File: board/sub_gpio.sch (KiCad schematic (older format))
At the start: 0 parts

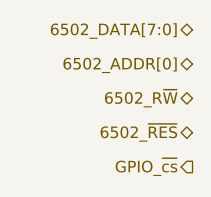
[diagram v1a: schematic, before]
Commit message: Level converters complete, display almost done
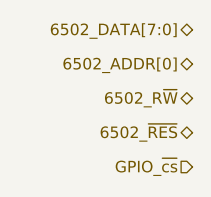
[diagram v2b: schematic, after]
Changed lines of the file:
@@
 $Descr A4 11693 8268
 encoding utf-8
-Sheet 4 10
+Sheet 4 15
 Title ""
 Date ""
@@
 Comment2 ""
 Comment3 ""
-Comment4 ""
+Comment4 "Quokka 6502 Microprocessor Trainer"
 $EndDescr
 Text HLabel 3650 1950 0    50   3State ~ 0
@@
 Text HLabel 3650 2100 0    50   BiDi ~ 0
 6502_ADDR[0]
-Text HLabel 3650 2550 0    50   Output ~ 0
+Text HLabel 3650 2550 0    50   Input ~ 0
 GPIO_~cs
 Text HLabel 3650 2400 0    50   BiDi ~ 0

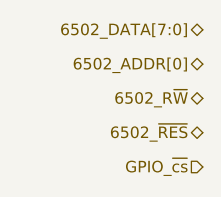
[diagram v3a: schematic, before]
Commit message: Bus signal connectivity rebuilt
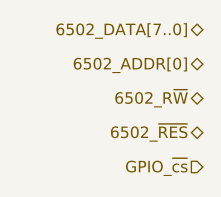
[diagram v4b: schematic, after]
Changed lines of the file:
@@
 $EndDescr
 Text HLabel 3650 1950 0    50   3State ~ 0
-6502_DATA[7:0]
+6502_DATA[7..0]
 Text HLabel 3650 2250 0    50   BiDi ~ 0
 6502_R~W

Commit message: gpio done
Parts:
- added C401, C?: 1u, symbol Device:C
- added D401, D?: DF5A6.8F, Package_TO_SOT_SMD:SOT-353_SC-70-5, symbol Power_Protection:SP0504BAJT
- added D402, D403, D404, D405, D406, D407, D408, D409: LED_Small, symbol Device:LED_Small
- added J401: Conn_01x08, symbol Connector_Generic:Conn_01x08
- added R401, R402, R403, R404, R405, R406, R407, R408: 160, symbol Device:R
- added U401: 74LVC4245A, symbol quokka:74LVC4245A
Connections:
- new net: D409.2 (A), D?.1 (K), J401.1 (Pin_1), U401.10 (GND)
- new net: D401.5 (K), D402.2 (A), J401.8 (Pin_8), U401.3 (A0)
- new net: D401.4 (K), D403.2 (A), J401.7 (Pin_7), U401.4 (A1)
- new net: D401.3 (K), D404.2 (A), J401.6 (Pin_6), U401.5 (A2)
- new net: D401.1 (K), D405.2 (A), J401.5 (Pin_5), U401.6 (A3)
- new net: D406.2 (A), D?.5 (K), J401.4 (Pin_4), U401.7 (A4)
- new net: D407.2 (A), D?.4 (K), J401.3 (Pin_3), U401.8 (A5)
- new net: D408.2 (A), D?.3 (K), J401.2 (Pin_2), U401.9 (A6)
- new net: D402.1 (K), R401.1
- new net: D409.1 (K), R408.1
- new net: D408.1 (K), R407.1
- new net: D407.1 (K), R406.1
- new net: D406.1 (K), R405.1
- new net: D405.1 (K), R404.1
- new net: D404.1 (K), R403.1
- new net: D403.1 (K), R402.1
- new net +3V3: C?.1, U401.23 (VCCB), U401.24 (VCCB)
- new net +5V: C401.1, U401.1 (VCCA)
- new net G0: U401.21 (B0)
- new net G1: U401.20 (B1)
- new net G2: U401.19 (B2)
- new net G3: U401.18 (B3)
- new net G4: U401.17 (B4)
- new net G5: U401.16 (B5)
- new net G6: U401.15 (B6)
- new net G7: U401.14 (B7)
- new net GND: C401.2, C?.2, D401.2 (A), D?.2 (A), R401.2, R402.2, R403.2, R404.2, R405.2, R406.2, R407.2, R408.2, U401.10 (GND), U401.12 (GND), U401.13 (GND), U401.22 (CE)
- new net R~W: U401.2 (A->B)
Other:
- note added: "Bidirectional Data"

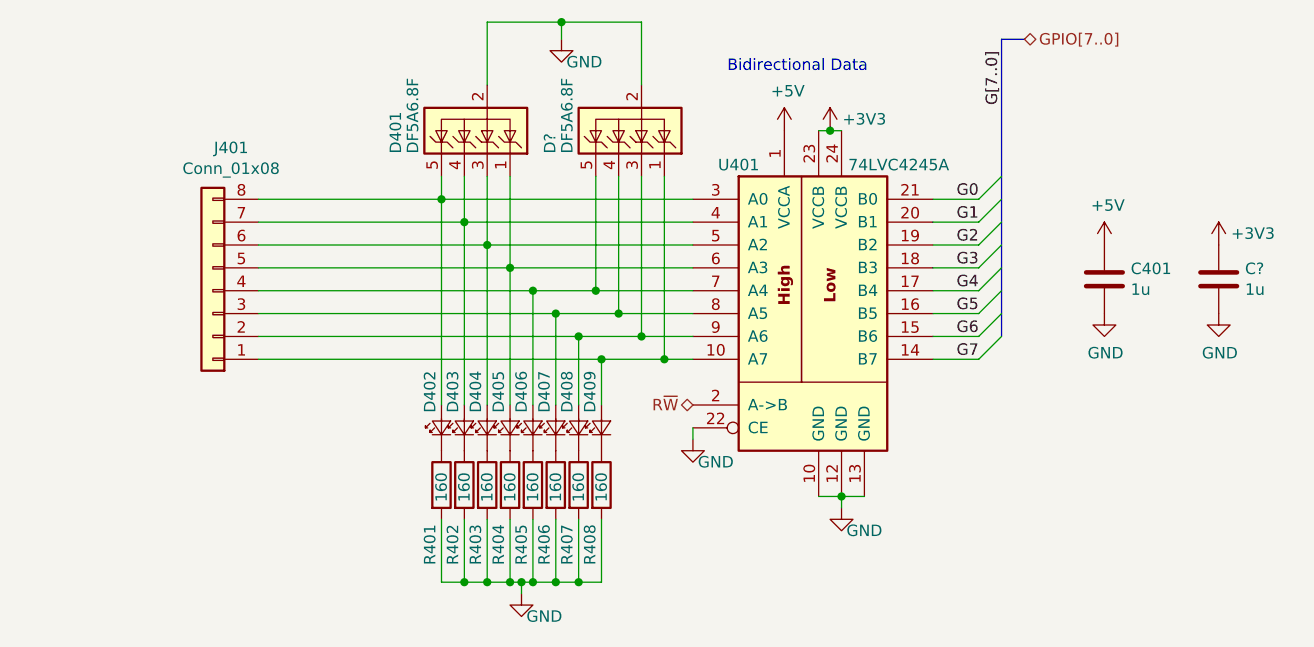
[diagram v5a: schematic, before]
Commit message: made some changes based on projected power budget
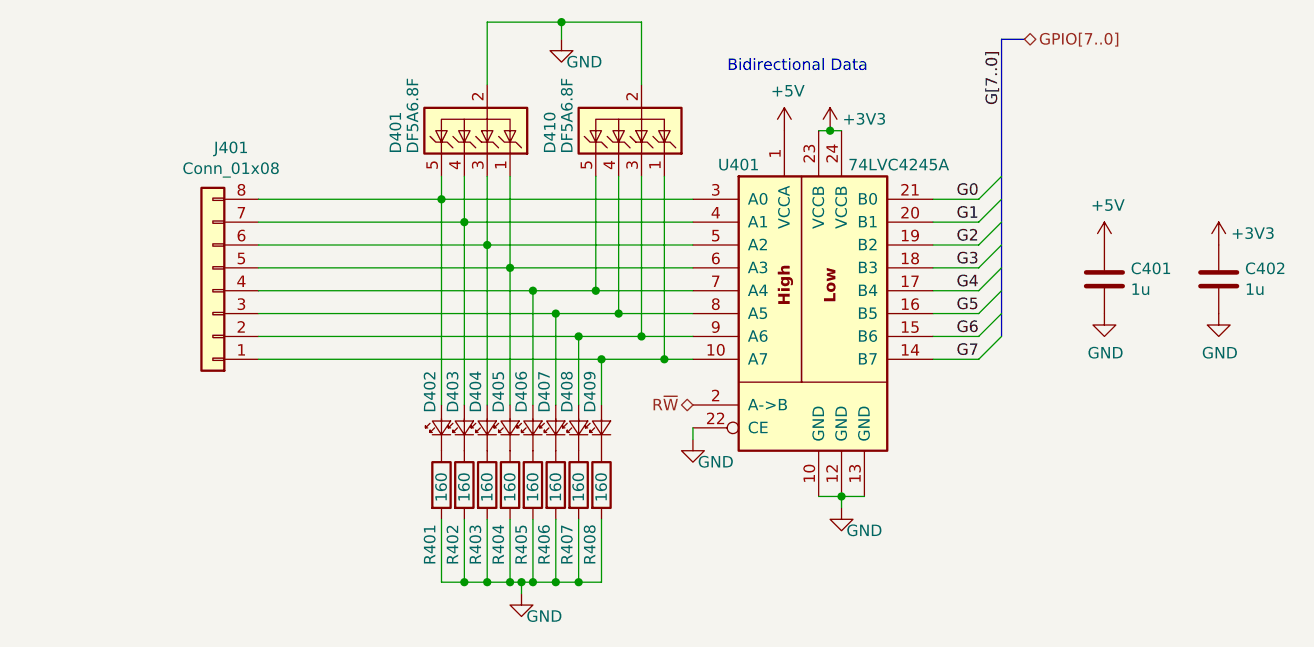
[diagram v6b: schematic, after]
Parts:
- gave numbers to parts that had none: 2
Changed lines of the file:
@@
 $EndComp
 $Comp
-L Power_Protection:SP0504BAJT D?
+L Power_Protection:SP0504BAJT D410
 U 1 1 5ABECE71
 P 4775 2200
-F 0 "D?" V 5175 2300 50  0000 R CNN
+F 0 "D410" V 5175 2300 50  0000 R CNN
 F 1 "DF5A6.8F" V 5100 2300 50  0000 R CNN
 F 2 "Package_TO_SOT_SMD:SOT-353_SC-70-5" H 5075 2150 50  0001 L CNN
@@
 	3900 2400 3900 2500
 $Comp
-L power:GND #PWR?
+L power:GND #PWR0408
 U 1 1 5AC0745E
 P 4425 1800
-F 0 "#PWR?" H 4425 1550 50  0001 C CNN
+F 0 "#PWR0408" H 4425 1550 50  0001 C CNN
 F 1 "GND" H 4525 1700 50  0000 C CNN
 F 2 "" H 4425 1800 50  0001 C CNN
@@
 Connection ~ 4425 1725
 $Comp
-L power:GND #PWR?
+L power:GND #PWR0407
 U 1 1 5AC0C5ED
 P 4250 4225
-F 0 "#PWR?" H 4250 3975 50  0001 C CNN
+F 0 "#PWR0407" H 4250 3975 50  0001 C CNN
 F 1 "GND" H 4350 4125 50  0000 C CNN
 F 2 "" H 4250 4225 50  0001 C CNN
@@
 	4250 4175 4300 4175
 $Comp
-L Device:C C?
+L Device:C C402
 U 1 1 5AC1AF1D
 P 7300 2850
-F 0 "C?" H 7415 2896 50  0000 L CNN
+F 0 "C402" H 7415 2896 50  0000 L CNN
 F 1 "1u" H 7415 2805 50  0000 L CNN
 F 2 "" H 7338 2700 50  0001 C CNN
@@
 $EndComp
 $Comp
-L power:GND #PWR?
+L power:GND #PWR0410
 U 1 1 5AC1AF23
 P 7300 3000
-F 0 "#PWR?" H 7300 2750 50  0001 C CNN
+F 0 "#PWR0410" H 7300 2750 50  0001 C CNN
 F 1 "GND" H 7305 2827 50  0000 C CNN
 F 2 "" H 7300 3000 50  0001 C CNN
@@
 	1    0    0    -1
 $EndComp
-Wire Bus Line
-	6350 1800 6350 3100
-$Comp
-L power:+3V3 #PWR?
+$Comp
+L power:+3V3 #PWR0409
 U 1 1 5AC1C826
 P 7300 2700
-F 0 "#PWR?" H 7300 2550 50  0001 C CNN
+F 0 "#PWR0409" H 7300 2550 50  0001 C CNN
 F 1 "+3V3" H 7450 2750 50  0000 C CNN
 F 2 "" H 7300 2700 50  0001 C CNN
@@
 	1    0    0    -1
 $EndComp
+Wire Bus Line
+	6350 1800 6350 3100
 $EndSCHEMATC

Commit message: Schematics mostly complete
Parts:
- removed J401: Conn_01x08, symbol Connector_Generic:Conn_01x08
- added J401: Conn_01x09, symbol Connector_Generic:Conn_01x09
- R401, R402, R403, R404, R405, R406, R407, R408: value 160 -> 390
- renumbered D410 to D402, D402 to D403, D403 to D404, D404 to D405, D405 to D406, D406 to D407, D407 to D408, D408 to D409, D409 to D410
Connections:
- net GND: now also J401.9 (Pin_9)
- net at D402.1 (K), D410.2 (A), U401.10 (GND): now also J401.8 (Pin_8)
- net at D401.5 (K), D403.2 (A), U401.3 (A0): now also J401.1 (Pin_1)
- net at D401.4 (K), D404.2 (A), U401.4 (A1): now also J401.2 (Pin_2)
- net at D401.3 (K), D405.2 (A), U401.5 (A2): now also J401.3 (Pin_3)
- net at D401.1 (K), D406.2 (A), U401.6 (A3): now also J401.4 (Pin_4)
- net at D402.5 (K), D407.2 (A), U401.7 (A4): now also J401.5 (Pin_5)
- net at D402.4 (K), D408.2 (A), U401.8 (A5): now also J401.6 (Pin_6)
- net at D402.3 (K), D409.2 (A), U401.9 (A6): now also J401.7 (Pin_7)
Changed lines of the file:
@@
 GPIO[7..0]
 $Comp
-L power:GND #PWR0404
+L power:GND #PWR0410
 U 1 1 5ABD3089
 P 5650 3850
-F 0 "#PWR0404" H 5650 3600 50  0001 C CNN
+F 0 "#PWR0410" H 5650 3600 50  0001 C CNN
 F 1 "GND" H 5750 3750 50  0000 C CNN
 F 2 "" H 5650 3850 50  0001 C CNN
@@
 G[7..0]
 $Comp
-L power:GND #PWR0401
+L power:GND #PWR0409
 U 1 1 5ABD3633
 P 5000 3550
-F 0 "#PWR0401" H 5000 3300 50  0001 C CNN
+F 0 "#PWR0409" H 5000 3300 50  0001 C CNN
 F 1 "GND" H 5100 3450 50  0000 C CNN
 F 2 "" H 5000 3550 50  0001 C CNN
@@
 $EndComp
 $Comp
-L power:+5V #PWR0405
+L power:+5V #PWR0404
 U 1 1 5ABD4DE4
 P 6800 2700
-F 0 "#PWR0405" H 6800 2550 50  0001 C CNN
+F 0 "#PWR0404" H 6800 2550 50  0001 C CNN
 F 1 "+5V" H 6815 2873 50  0000 C CNN
 F 2 "" H 6800 2700 50  0001 C CNN
@@
 $EndComp
 $Comp
-L Connector_Generic:Conn_01x08 J401
-U 1 1 5ABD5411
-P 2900 2900
-F 0 "J401" H 2820 2275 50  0000 C CNN
-F 1 "Conn_01x08" H 2820 2366 50  0000 C CNN
-F 2 "" H 2900 2900 50  0001 C CNN
-F 3 "~" H 2900 2900 50  0001 C CNN
-	1    2900 2900
-	-1   0    0    1
-$EndComp
-$Comp
-L Device:LED_Small D402
+L Device:LED_Small D403
 U 1 1 5ABE75BA
 P 3900 3500
-F 0 "D402" H 4150 3550 50  0000 R CNN
+F 0 "D403" H 4150 3550 50  0000 R CNN
 F 1 "LED_Small" V 3855 3432 50  0001 R CNN
 F 2 "" V 3900 3500 50  0001 C CNN
@@
 $EndComp
 $Comp
-L Device:LED_Small D409
+L Device:LED_Small D410
 U 1 1 5ABE75EB
 P 4600 3500
-F 0 "D409" H 4850 3550 50  0000 R CNN
+F 0 "D410" H 4850 3550 50  0000 R CNN
 F 1 "LED_Small" V 4555 3432 50  0001 R CNN
 F 2 "" V 4600 3500 50  0001 C CNN
@@
 $EndComp
 $Comp
-L Device:LED_Small D408
+L Device:LED_Small D409
 U 1 1 5ABE75F2
 P 4500 3500
-F 0 "D408" H 4750 3550 50  0000 R CNN
+F 0 "D409" H 4750 3550 50  0000 R CNN
 F 1 "LED_Small" V 4455 3432 50  0001 R CNN
 F 2 "" V 4500 3500 50  0001 C CNN
@@
 $EndComp
 $Comp
-L Device:LED_Small D407
+L Device:LED_Small D408
 U 1 1 5ABE75F9
 P 4400 3500
-F 0 "D407" H 4650 3550 50  0000 R CNN
+F 0 "D408" H 4650 3550 50  0000 R CNN
 F 1 "LED_Small" V 4355 3432 50  0001 R CNN
 F 2 "" V 4400 3500 50  0001 C CNN
@@
 $EndComp
 $Comp
-L Device:LED_Small D406
+L Device:LED_Small D407
 U 1 1 5ABE7600
 P 4300 3500
-F 0 "D406" H 4550 3550 50  0000 R CNN
+F 0 "D407" H 4550 3550 50  0000 R CNN
 F 1 "LED_Small" V 4255 3432 50  0001 R CNN
 F 2 "" V 4300 3500 50  0001 C CNN
@@
 $EndComp
 $Comp
-L Device:LED_Small D405
+L Device:LED_Small D406
 U 1 1 5ABE7607
 P 4200 3500
-F 0 "D405" H 4450 3550 50  0000 R CNN
+F 0 "D406" H 4450 3550 50  0000 R CNN
 F 1 "LED_Small" V 4155 3432 50  0001 R CNN
 F 2 "" V 4200 3500 50  0001 C CNN
@@
 $EndComp
 $Comp
-L Device:LED_Small D404
+L Device:LED_Small D405
 U 1 1 5ABE760E
 P 4100 3500
-F 0 "D404" H 4350 3550 50  0000 R CNN
+F 0 "D405" H 4350 3550 50  0000 R CNN
 F 1 "LED_Small" V 4055 3432 50  0001 R CNN
 F 2 "" V 4100 3500 50  0001 C CNN
@@
 $EndComp
 $Comp
-L Device:LED_Small D403
+L Device:LED_Small D404
 U 1 1 5ABE7615
 P 4000 3500
-F 0 "D403" H 4250 3550 50  0000 R CNN
+F 0 "D404" H 4250 3550 50  0000 R CNN
 F 1 "LED_Small" V 3955 3432 50  0001 R CNN
 F 2 "" V 4000 3500 50  0001 C CNN
@@
 P 3900 3750
 F 0 "R401" V 3850 3400 50  0000 L CNN
-F 1 "160" V 3900 3675 50  0000 L CNN
+F 1 "390" V 3900 3675 50  0000 L CNN
 F 2 "" V 3830 3750 50  0001 C CNN
 F 3 "~" H 3900 3750 50  0001 C CNN
@@
 P 4000 3750
 F 0 "R402" V 3950 3400 50  0000 L CNN
-F 1 "160" V 4000 3675 50  0000 L CNN
+F 1 "390" V 4000 3675 50  0000 L CNN
 F 2 "" V 3930 3750 50  0001 C CNN
 F 3 "~" H 4000 3750 50  0001 C CNN
@@
 P 4100 3750
 F 0 "R403" V 4050 3400 50  0000 L CNN
-F 1 "160" V 4100 3675 50  0000 L CNN
+F 1 "390" V 4100 3675 50  0000 L CNN
 F 2 "" V 4030 3750 50  0001 C CNN
 F 3 "~" H 4100 3750 50  0001 C CNN
@@
 P 4200 3750
 F 0 "R404" V 4150 3400 50  0000 L CNN
-F 1 "160" V 4200 3675 50  0000 L CNN
+F 1 "390" V 4200 3675 50  0000 L CNN
 F 2 "" V 4130 3750 50  0001 C CNN
 F 3 "~" H 4200 3750 50  0001 C CNN
@@
 P 4300 3750
 F 0 "R405" V 4250 3400 50  0000 L CNN
-F 1 "160" V 4300 3675 50  0000 L CNN
+F 1 "390" V 4300 3675 50  0000 L CNN
 F 2 "" V 4230 3750 50  0001 C CNN
 F 3 "~" H 4300 3750 50  0001 C CNN
@@
 P 4400 3750
 F 0 "R406" V 4350 3400 50  0000 L CNN
-F 1 "160" V 4400 3675 50  0000 L CNN
+F 1 "390" V 4400 3675 50  0000 L CNN
 F 2 "" V 4330 3750 50  0001 C CNN
 F 3 "~" H 4400 3750 50  0001 C CNN
@@
 P 4500 3750
 F 0 "R407" V 4450 3400 50  0000 L CNN
-F 1 "160" V 4500 3675 50  0000 L CNN
+F 1 "390" V 4500 3675 50  0000 L CNN
 F 2 "" V 4430 3750 50  0001 C CNN
 F 3 "~" H 4500 3750 50  0001 C CNN
@@
 P 4600 3750
 F 0 "R408" V 4550 3400 50  0000 L CNN
-F 1 "160" V 4600 3675 50  0000 L CNN
+F 1 "390" V 4600 3675 50  0000 L CNN
 F 2 "" V 4530 3750 50  0001 C CNN
 F 3 "~" H 4600 3750 50  0001 C CNN
@@
 $EndComp
 $Comp
-L Power_Protection:SP0504BAJT D410
+L Power_Protection:SP0504BAJT D402
 U 1 1 5ABECE71
 P 4775 2200
-F 0 "D410" V 5175 2300 50  0000 R CNN
+F 0 "D402" V 5175 2300 50  0000 R CNN
 F 1 "DF5A6.8F" V 5100 2300 50  0000 R CNN
 F 2 "Package_TO_SOT_SMD:SOT-353_SC-70-5" H 5075 2150 50  0001 L CNN
@@
 	3900 2400 3900 2500
 $Comp
-L power:GND #PWR0408
+L power:GND #PWR0401
 U 1 1 5AC0745E
 P 4425 1800
-F 0 "#PWR0408" H 4425 1550 50  0001 C CNN
+F 0 "#PWR0401" H 4425 1550 50  0001 C CNN
 F 1 "GND" H 4525 1700 50  0000 C CNN
 F 2 "" H 4425 1800 50  0001 C CNN
@@
 Connection ~ 4425 1725
 $Comp
-L power:GND #PWR0407
+L power:GND #PWR0411
 U 1 1 5AC0C5ED
 P 4250 4225
-F 0 "#PWR0407" H 4250 3975 50  0001 C CNN
+F 0 "#PWR0411" H 4250 3975 50  0001 C CNN
 F 1 "GND" H 4350 4125 50  0000 C CNN
 F 2 "" H 4250 4225 50  0001 C CNN
@@
 $EndComp
 $Comp
-L power:GND #PWR0410
+L power:GND #PWR0407
 U 1 1 5AC1AF23
 P 7300 3000
-F 0 "#PWR0410" H 7300 2750 50  0001 C CNN
+F 0 "#PWR0407" H 7300 2750 50  0001 C CNN
 F 1 "GND" H 7305 2827 50  0000 C CNN
 F 2 "" H 7300 3000 50  0001 C CNN
@@
 $EndComp
 $Comp
-L power:+3V3 #PWR0409
+L power:+3V3 #PWR0405
 U 1 1 5AC1C826
 P 7300 2700
-F 0 "#PWR0409" H 7300 2550 50  0001 C CNN
-F 1 "+3V3" H 7450 2750 50  0000 C CNN
+F 0 "#PWR0405" H 7300 2550 50  0001 C CNN
+F 1 "+3V3" H 7300 2875 50  0000 C CNN
 F 2 "" H 7300 2700 50  0001 C CNN
 F 3 "" H 7300 2700 50  0001 C CNN
@@
 	1    0    0    -1
 $EndComp
+$Comp
+L Connector_Generic:Conn_01x09 J401
+U 1 1 5ACF6504
+P 2900 2900
+F 0 "J401" H 2820 3517 50  0000 C CNN
+F 1 "Conn_01x09" H 2820 3426 50  0000 C CNN
+F 2 "" H 2900 2900 50  0001 C CNN
+F 3 "~" H 2900 2900 50  0001 C CNN
+	1    2900 2900
+	-1   0    0    -1
+$EndComp
+$Comp
+L power:GND #PWR0408
+U 1 1 5ACF822D
+P 3150 3350
+F 0 "#PWR0408" H 3150 3100 50  0001 C CNN
+F 1 "GND" H 3155 3177 50  0000 C CNN
+F 2 "" H 3150 3350 50  0001 C CNN
+F 3 "" H 3150 3350 50  0001 C CNN
+	1    3150 3350
+	1    0    0    -1
+$EndComp
+Wire Wire Line
+	3150 3350 3150 3300
+Wire Wire Line
+	3150 3300 3100 3300
 Wire Bus Line
 	6350 1800 6350 3100

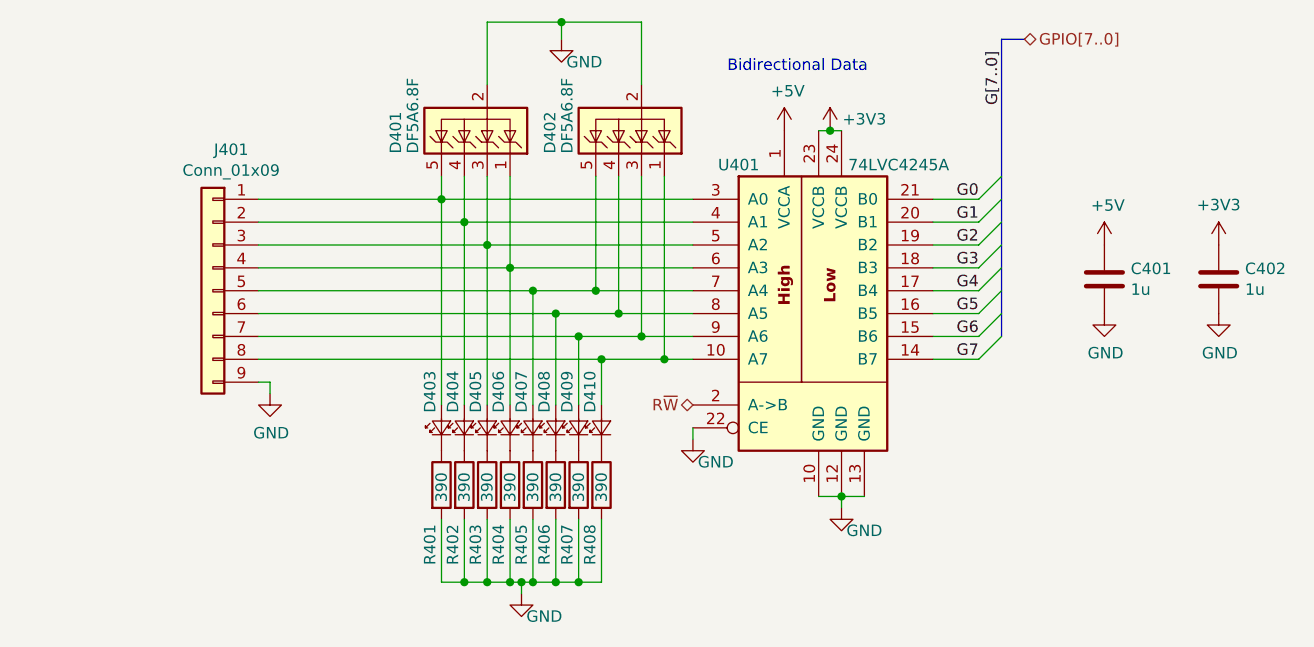
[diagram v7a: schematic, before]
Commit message: Started picking footprints. Merged many components.
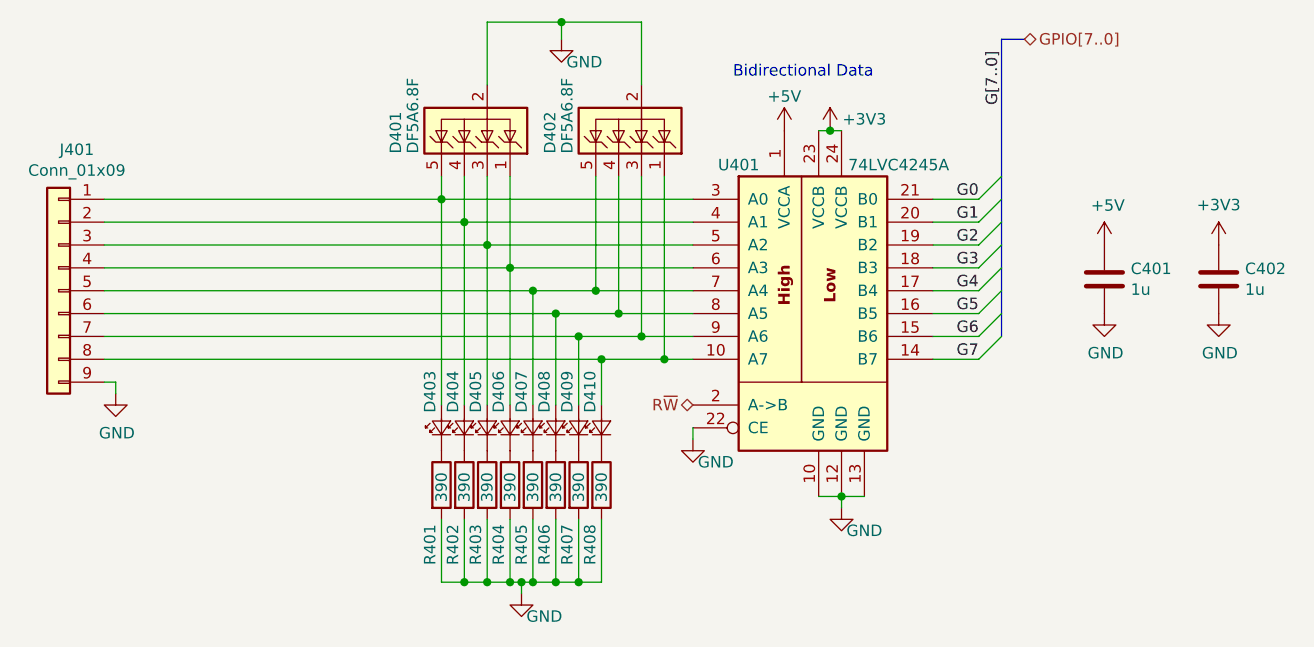
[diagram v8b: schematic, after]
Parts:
- U401: footprint (none) -> Package_SO:TSSOP-24_4.4x7.8mm_P0.65mm
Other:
- moved on the sheet: J401
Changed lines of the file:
@@
 $Descr A4 11693 8268
 encoding utf-8
-Sheet 4 14
+Sheet 4 15
 Title ""
 Date ""
@@
 P 5400 2200
 F 0 "#PWR0402" H 5400 2050 50  0001 C CNN
-F 1 "+5V" H 5415 2373 50  0000 C CNN
+F 1 "+5V" H 5400 2350 50  0000 C CNN
 F 2 "" H 5400 2200 50  0001 C CNN
 F 3 "" H 5400 2200 50  0001 C CNN
@@
 F 0 "U401" H 5200 3650 50  0000 C CNN
 F 1 "74LVC4245A" H 5900 3650 50  0000 C CNN
-F 2 "" H 5500 3000 50  0001 C CNN
+F 2 "Package_SO:TSSOP-24_4.4x7.8mm_P0.65mm" H 5500 3000 50  0001 C CNN
 F 3 "https://assets.nexperia.com/documents/data-sheet/74LVC4245A.pdf" H 5500 3000 50  0001 C CNN
 	1    5500 3000
 	1    0    0    -1
 $EndComp
-Text Notes 5150 1950 0    50   ~ 0
+Text Notes 5175 1975 0    50   ~ 0
 Bidirectional Data
 Entry Wire Line
@@
 	5000 2700 4100 2700
 Wire Wire Line
-	3100 2500 3900 2500
-Wire Wire Line
-	3100 2900 4300 2900
-Wire Wire Line
-	3100 3100 4500 3100
+	2425 2500 3900 2500
+Wire Wire Line
+	2425 2900 4300 2900
+Wire Wire Line
+	2425 3100 4500 3100
 Wire Wire Line
 	4600 3400 4600 3200
 Connection ~ 4600 3200
 Wire Wire Line
-	4600 3200 3100 3200
+	4600 3200 2425 3200
 Wire Wire Line
 	4500 3400 4500 3100
@@
 Connection ~ 4400 3000
 Wire Wire Line
-	4400 3000 3100 3000
+	4400 3000 2425 3000
 Wire Wire Line
 	4300 3400 4300 2900
@@
 	4000 2600 5000 2600
 Wire Wire Line
-	3100 2800 4200 2800
+	2425 2800 4200 2800
 Wire Wire Line
 	4100 2700 4100 3400
 Connection ~ 4100 2700
 Wire Wire Line
-	4100 2700 3100 2700
+	4100 2700 2425 2700
 Wire Wire Line
 	3900 3400 3900 2500
@@
 	3900 2500 5000 2500
 Wire Wire Line
-	3100 2600 4000 2600
+	2425 2600 4000 2600
 Wire Wire Line
 	4300 2900 4575 2900
@@
 L Connector_Generic:Conn_01x09 J401
 U 1 1 5ACF6504
-P 2900 2900
-F 0 "J401" H 2820 3517 50  0000 C CNN
-F 1 "Conn_01x09" H 2820 3426 50  0000 C CNN
-F 2 "" H 2900 2900 50  0001 C CNN
-F 3 "~" H 2900 2900 50  0001 C CNN
-	1    2900 2900
+P 2225 2900
+F 0 "J401" H 2145 3517 50  0000 C CNN
+F 1 "Conn_01x09" H 2145 3426 50  0000 C CNN
+F 2 "" H 2225 2900 50  0001 C CNN
+F 3 "~" H 2225 2900 50  0001 C CNN
+	1    2225 2900
 	-1   0    0    -1
 $EndComp
@@
 L power:GND #PWR0408
 U 1 1 5ACF822D
-P 3150 3350
-F 0 "#PWR0408" H 3150 3100 50  0001 C CNN
-F 1 "GND" H 3155 3177 50  0000 C CNN
-F 2 "" H 3150 3350 50  0001 C CNN
-F 3 "" H 3150 3350 50  0001 C CNN
-	1    3150 3350
-	1    0    0    -1
-$EndComp
-Wire Wire Line
-	3150 3350 3150 3300
-Wire Wire Line
-	3150 3300 3100 3300
+P 2475 3350
+F 0 "#PWR0408" H 2475 3100 50  0001 C CNN
+F 1 "GND" H 2480 3177 50  0000 C CNN
+F 2 "" H 2475 3350 50  0001 C CNN
+F 3 "" H 2475 3350 50  0001 C CNN
+	1    2475 3350
+	1    0    0    -1
+$EndComp
+Wire Wire Line
+	2475 3350 2475 3300
+Wire Wire Line
+	2475 3300 2425 3300
 Wire Bus Line
 	6350 1800 6350 3100
